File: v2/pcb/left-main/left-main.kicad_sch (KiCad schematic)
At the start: 33 parts, among them J1 Conn_01x10, SW1 SW_Push, SW10 SW_Push, SW11 SW_Push, SW12 SW_Push, SW13 SW_Push, SW14 SW_Push, SW15 SW_Push, SW16 SW_Push, SW2 SW_Push, SW3 SW_Push, SW4 SW_Push, SW5 SW_Push, SW6 SW_Push, SW7 SW_Push, SW8 SW_Push, SW9 SW_Push

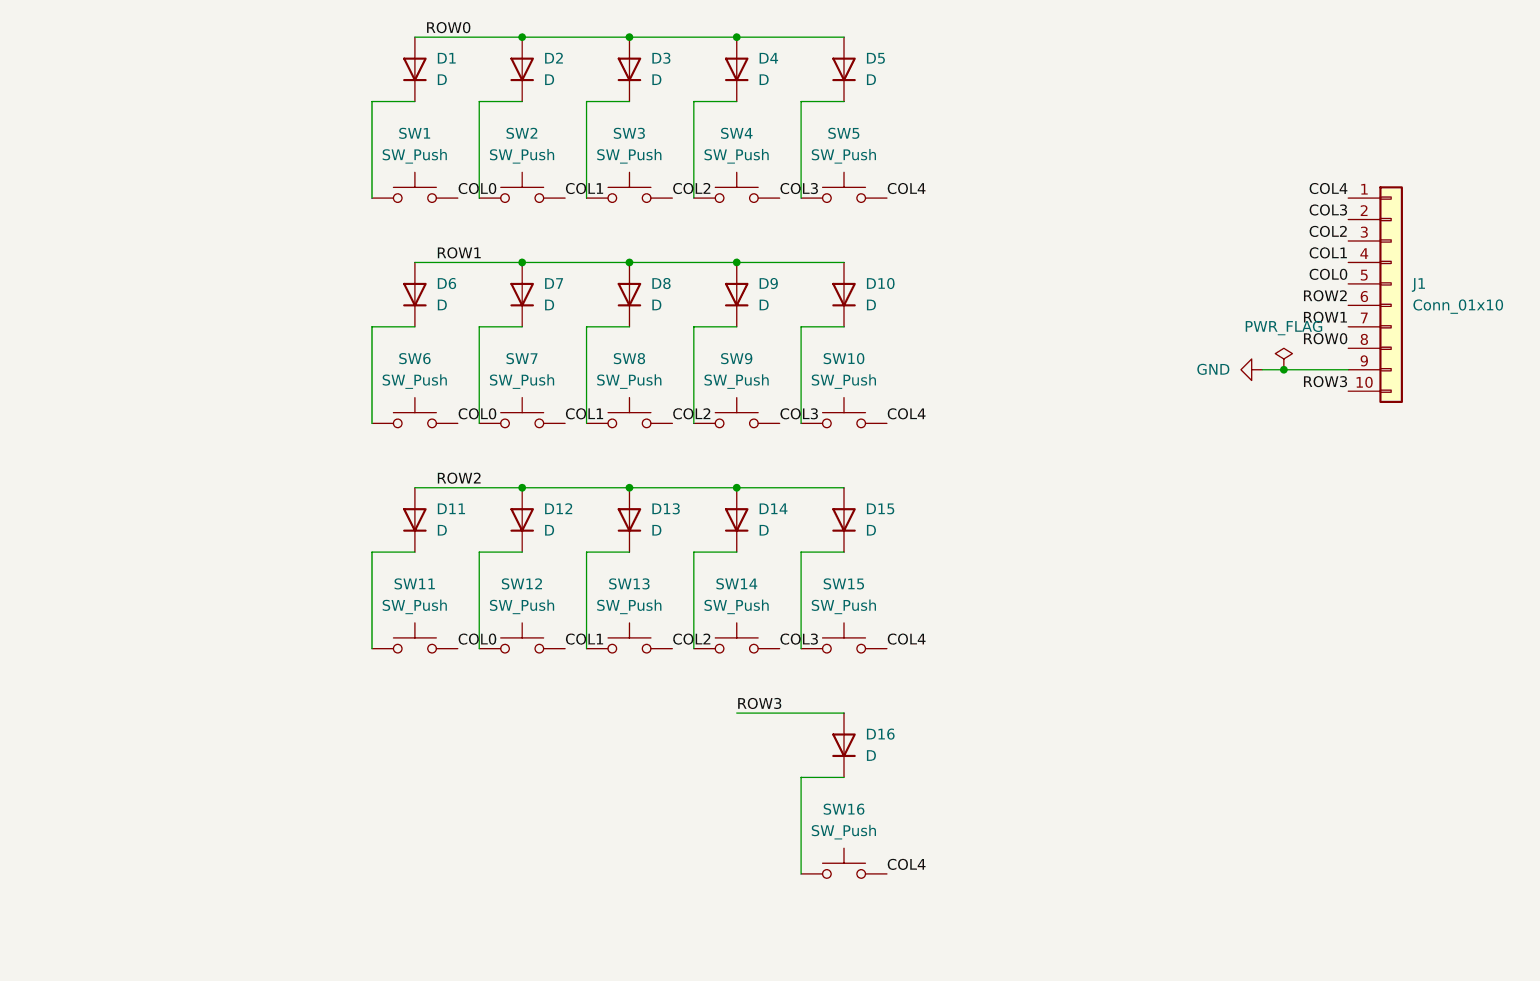
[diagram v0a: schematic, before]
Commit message: feat: add left main pcb
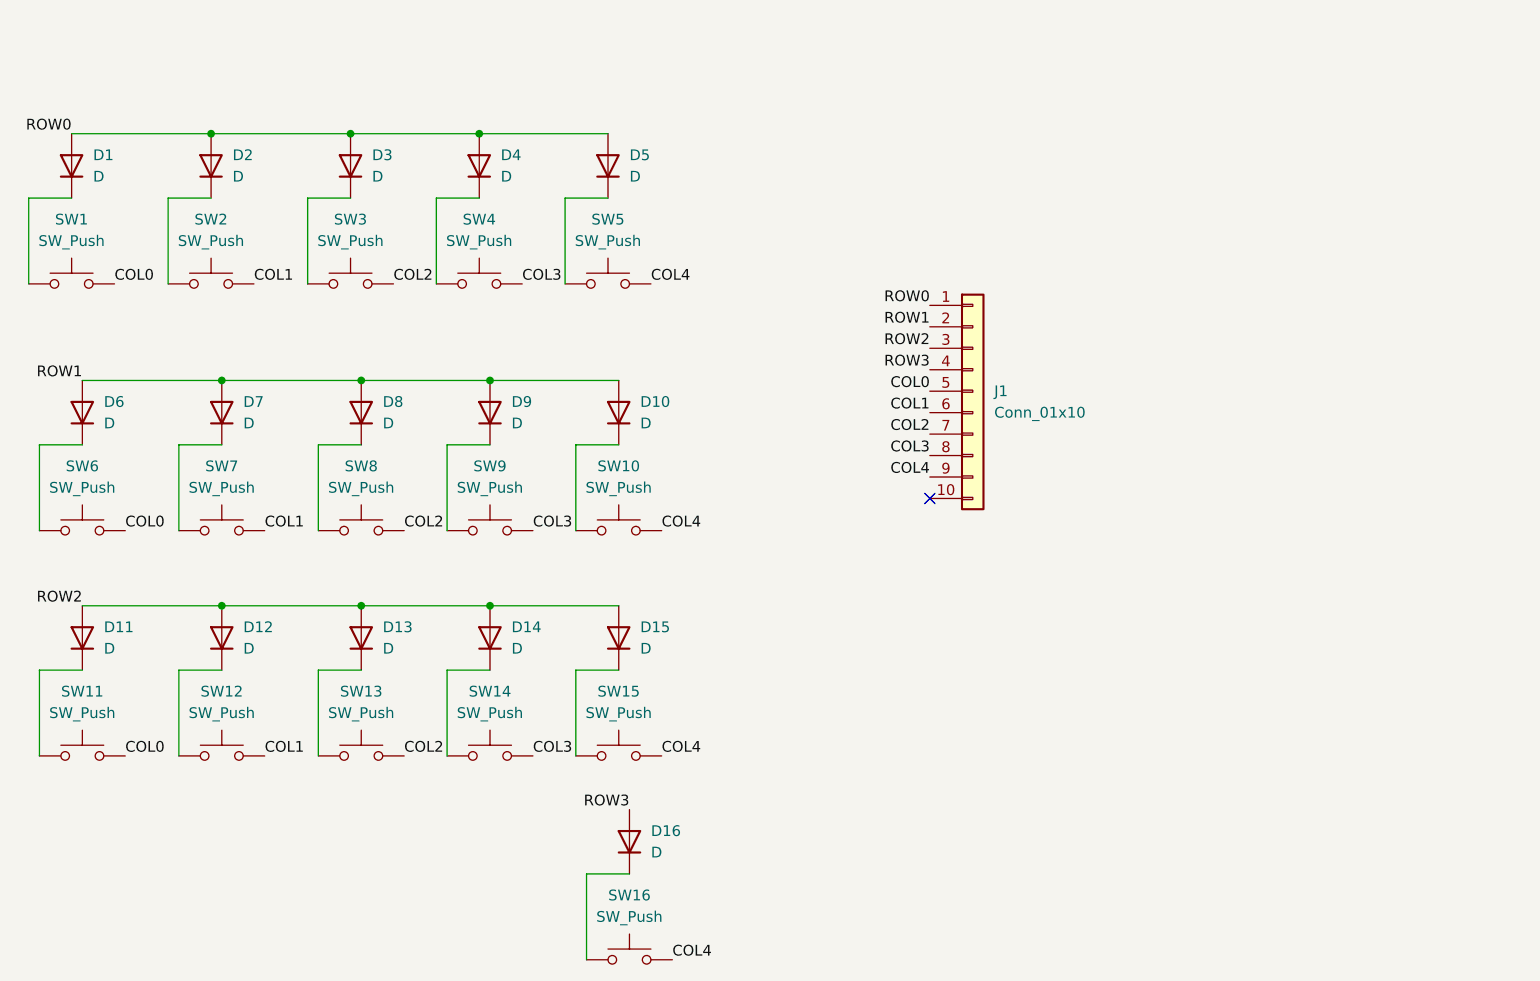
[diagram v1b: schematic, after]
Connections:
- net GND is gone; now on net COL4: J1.9 (Pin_9)
- net COL1: now also J1.6 (Pin_6); no longer J1.4 (Pin_4)
- net COL2: now also J1.7 (Pin_7); no longer J1.3 (Pin_3)
- net COL3: now also J1.8 (Pin_8); no longer J1.2 (Pin_2)
- net COL4: no longer J1.1 (Pin_1)
- net ROW0: now also J1.1 (Pin_1); no longer J1.8 (Pin_8)
- net ROW1: now also J1.2 (Pin_2); no longer J1.7 (Pin_7)
- net ROW2: now also J1.3 (Pin_3); no longer J1.6 (Pin_6)
- net ROW3: now also J1.4 (Pin_4); no longer J1.10 (Pin_10)
- no-connect marks 0 -> 1
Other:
- title: kobu2 left-main -> (none)
